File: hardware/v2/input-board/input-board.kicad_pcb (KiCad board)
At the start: 2 copper layers, 110 x 46 mm, 30 parts, among them J27 Screw_Terminal_01x16

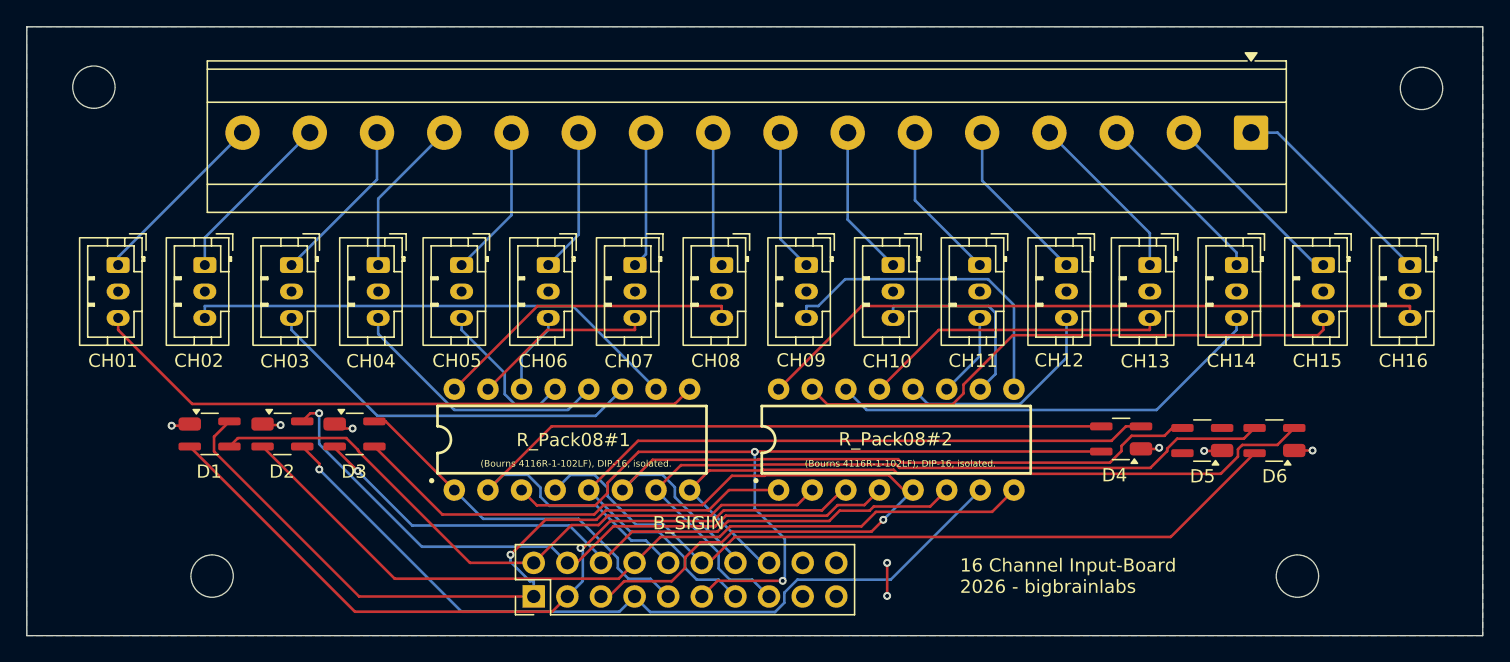
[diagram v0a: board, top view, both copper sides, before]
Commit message: Hardware v2: Input-Board neu generiert (Rev.1/Rev.2)
Gerber neu erzeugt, rev1/rev2-ZIP und Pick-&-Place-CSV ergänzt,
Schaltplan/Layout und Projektdateien aktualisiert.

Co-Authored-By: Claude Opus 4.8 <noreply@anthropic.com>
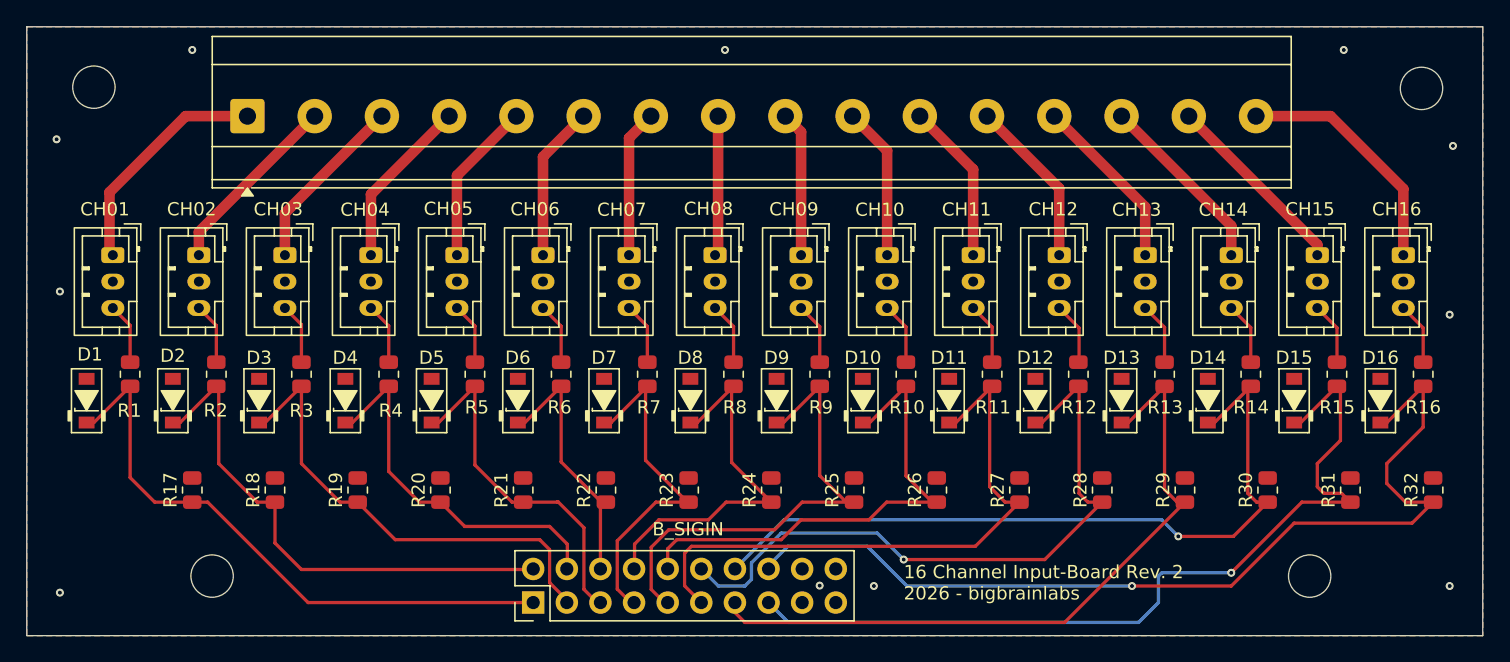
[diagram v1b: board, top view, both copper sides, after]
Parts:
- removed R_Pack08#1, R_Pack08#2: R_Pack08, PCM_SparkFun-Semiconductor-Standard:DIP-16
- added D10: D_Zener, PCM_Diode_SMD_AKL:D_SOD-123_Zener, F.Cu at (166.2, 70.8)
- added D11: D_Zener, PCM_Diode_SMD_AKL:D_SOD-123_Zener, F.Cu at (172.7, 70.8)
- added D12: D_Zener, PCM_Diode_SMD_AKL:D_SOD-123_Zener, F.Cu at (179.2, 70.8)
- added D13: D_Zener, PCM_Diode_SMD_AKL:D_SOD-123_Zener, F.Cu at (185.7, 70.8)
- added D14: D_Zener, PCM_Diode_SMD_AKL:D_SOD-123_Zener, F.Cu at (192.2, 70.8)
- added D15: D_Zener, PCM_Diode_SMD_AKL:D_SOD-123_Zener, F.Cu at (198.8, 70.8)
- added D16: D_Zener, PCM_Diode_SMD_AKL:D_SOD-123_Zener, F.Cu at (205.3, 70.8)
- added D7: D_Zener, PCM_Diode_SMD_AKL:D_SOD-123_Zener, F.Cu at (146.6, 70.8)
- added D8: D_Zener, PCM_Diode_SMD_AKL:D_SOD-123_Zener, F.Cu at (153.1, 70.8)
- added D9: D_Zener, PCM_Diode_SMD_AKL:D_SOD-123_Zener, F.Cu at (159.7, 70.8)
- added R1: 1k, Resistor_SMD:R_0805_2012Metric, F.Cu at (110.8, 68.8)
- added R10: 1k, Resistor_SMD:R_0805_2012Metric, F.Cu at (169.4, 68.8)
- added R11: 1k, Resistor_SMD:R_0805_2012Metric, F.Cu at (175.9, 68.8)
- added R12: 1k, Resistor_SMD:R_0805_2012Metric, F.Cu at (182.4, 68.8)
- added R13: 1k, Resistor_SMD:R_0805_2012Metric, F.Cu at (189.0, 68.8)
- added R14: 1k, Resistor_SMD:R_0805_2012Metric, F.Cu at (195.5, 68.8)
- added R15: 1k, Resistor_SMD:R_0805_2012Metric, F.Cu at (202.0, 68.8)
- added R16: 1k, Resistor_SMD:R_0805_2012Metric, F.Cu at (208.5, 68.8)
- added R17: 1M, Resistor_SMD:R_0805_2012Metric, F.Cu at (115.5, 77.5)
- added R18: 1M, Resistor_SMD:R_0805_2012Metric, F.Cu at (121.8, 77.5)
- added R19: 1M, Resistor_SMD:R_0805_2012Metric, F.Cu at (128.0, 77.5)
- added R2: 1k, Resistor_SMD:R_0805_2012Metric, F.Cu at (117.3, 68.8)
- added R20: 1M, Resistor_SMD:R_0805_2012Metric, F.Cu at (134.2, 77.5)
- added R21: 1M, Resistor_SMD:R_0805_2012Metric, F.Cu at (140.5, 77.5)
- added R22: 1M, Resistor_SMD:R_0805_2012Metric, F.Cu at (146.8, 77.5)
- added R23: 1M, Resistor_SMD:R_0805_2012Metric, F.Cu at (153.0, 77.5)
- added R24: 1M, Resistor_SMD:R_0805_2012Metric, F.Cu at (159.2, 77.5)
- added R25: 1M, Resistor_SMD:R_0805_2012Metric, F.Cu at (165.5, 77.5)
- added R26: 1M, Resistor_SMD:R_0805_2012Metric, F.Cu at (171.8, 77.5)
- added R27: 1M, Resistor_SMD:R_0805_2012Metric, F.Cu at (178.0, 77.5)
- added R28: 1M, Resistor_SMD:R_0805_2012Metric, F.Cu at (184.2, 77.5)
- added R29: 1M, Resistor_SMD:R_0805_2012Metric, F.Cu at (190.5, 77.5)
- added R3: 1k, Resistor_SMD:R_0805_2012Metric, F.Cu at (123.8, 68.8)
- added R30: 1M, Resistor_SMD:R_0805_2012Metric, F.Cu at (196.8, 77.5)
- added R31: 1M, Resistor_SMD:R_0805_2012Metric, F.Cu at (203.0, 77.5)
- added R32: 1M, Resistor_SMD:R_0805_2012Metric, F.Cu at (209.2, 77.5)
- added R4: 1k, Resistor_SMD:R_0805_2012Metric, F.Cu at (130.3, 68.8)
- added R5: 1k, Resistor_SMD:R_0805_2012Metric, F.Cu at (136.9, 68.8)
- added R6: 1k, Resistor_SMD:R_0805_2012Metric, F.Cu at (143.4, 68.8)
- added R7: 1k, Resistor_SMD:R_0805_2012Metric, F.Cu at (149.9, 68.8)
- added R8: 1k, Resistor_SMD:R_0805_2012Metric, F.Cu at (156.4, 68.8)
- added R9: 1k, Resistor_SMD:R_0805_2012Metric, F.Cu at (162.9, 68.8)
- D1, D2, D3, D4, D5, D6: value SP0503BAHTG -> D_Zener; footprint Package_TO_SOT_SMD:SOT-143_Handsoldering -> PCM_Diode_SMD_AKL:D_SOD-123_Zener
- moved CH01 98.0 mm to (109.5, 59.8)
- moved CH16 97.1 mm to (207.0, 59.8)
- moved CH02 85.0 mm to (116.0, 59.8)
- moved CH15 84.1 mm to (200.5, 59.8)
- moved J27 75.8 mm to (119.7, 49.2), turned to 0 degrees
- moved CH03 71.9 mm to (122.5, 59.8)
- moved CH14 71.0 mm to (194.0, 59.8)
- moved CH04 58.9 mm to (129.0, 59.8)
- moved D4 58.7 mm to (127.1, 70.8), turned to 90 degrees
- moved D5 58.3 mm to (133.6, 70.8), turned to 90 degrees
- moved CH13 58.0 mm to (187.5, 59.8)
- moved D6 57.2 mm to (140.1, 70.8), turned to 90 degrees
- moved CH05 46.1 mm to (135.5, 59.8)
- moved CH12 45.2 mm to (181.0, 59.8)
- moved CH06 33.0 mm to (142.0, 59.8)
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- renumbered CH16 to CH01, CH15 to CH02, CH14 to CH03, CH13 to CH04, CH12 to CH05, CH11 to CH06, CH10 to CH07, CH09 to CH08, CH08 to CH09, CH07 to CH10, CH06 to CH11, CH05 to CH12, CH04 to CH13, CH03 to CH14, CH02 to CH15, CH01 to CH16
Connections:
- B_SIGIN pad 1: Net-(J29-Pin_1) -> Net-(D1-K)
- B_SIGIN pad 10: Net-(J29-Pin_10) -> Net-(D10-K)
- B_SIGIN pad 11: Net-(J29-Pin_11) -> Net-(D11-K)
- B_SIGIN pad 12: Net-(J29-Pin_12) -> Net-(D12-K)
- B_SIGIN pad 13: Net-(J29-Pin_13) -> Net-(D13-K)
- B_SIGIN pad 14: Net-(J29-Pin_14) -> Net-(D14-K)
- B_SIGIN pad 15: Net-(J29-Pin_15) -> Net-(D15-K)
- B_SIGIN pad 16: Net-(J29-Pin_16) -> Net-(D16-K)
- B_SIGIN pad 2: Net-(J29-Pin_2) -> Net-(D2-K)
- B_SIGIN pad 3: Net-(J29-Pin_3) -> Net-(D3-K)
- B_SIGIN pad 4: Net-(J29-Pin_4) -> Net-(D4-K)
- B_SIGIN pad 5: Net-(J29-Pin_5) -> Net-(D5-K)
- B_SIGIN pad 6: Net-(J29-Pin_6) -> Net-(D6-K)
- B_SIGIN pad 7: Net-(J29-Pin_7) -> Net-(D7-K)
- B_SIGIN pad 8: Net-(J29-Pin_8) -> Net-(D8-K)
- B_SIGIN pad 9: Net-(J29-Pin_9) -> Net-(D9-K)
- D1 pad 1: GND -> Net-(D1-K)
- D1 pad 2: Net-(J29-Pin_3) -> GND
- D2 pad 1: GND -> Net-(D2-K)
- D2 pad 2: Net-(J29-Pin_8) -> GND
- D3 pad 1: GND -> Net-(D3-K)
- D3 pad 2: Net-(J29-Pin_6) -> GND
- D4 pad 1: GND -> Net-(D4-K)
- D4 pad 2: Net-(J29-Pin_13) -> GND
- D5 pad 1: GND -> Net-(D5-K)
- D5 pad 2: unconnected-(D5-Pad2) -> GND
- D6 pad 1: GND -> Net-(D6-K)
- D6 pad 2: Net-(J29-Pin_16) -> GND
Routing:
- net Net-(J29-Pin_5): track 71.9 -> 0.00 mm, vias 1 -> 0
- net Net-(D16-K): track 0.00 -> 71.9 mm, vias 0 -> 1
- net Net-(J29-Pin_10): track 65.6 -> 0.00 mm
- net Net-(D15-K): track 0.00 -> 65.3 mm, vias 0 -> 1
- net Net-(J29-Pin_11): track 63.8 -> 0.00 mm, vias 2 -> 0
- net Net-(J29-Pin_8): track 63.7 -> 0.00 mm
- net Net-(J29-Pin_7): track 61.9 -> 0.00 mm, vias 1 -> 0
- net Net-(J29-Pin_3): track 60.3 -> 0.00 mm, vias 1 -> 0
- net Net-(J29-Pin_15): track 60.1 -> 0.00 mm
- net Net-(J29-Pin_12): track 59.9 -> 0.00 mm
- net Net-(J29-Pin_13): track 58.6 -> 0.00 mm
- net Net-(J29-Pin_1): track 57.8 -> 0.00 mm, vias 1 -> 0
- net Net-(D14-K): track 0.00 -> 57.7 mm, vias 0 -> 1
- net Net-(J29-Pin_14): track 57.1 -> 0.00 mm
- net Net-(J29-Pin_16): track 56.5 -> 0.00 mm
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- added copper zone on F.Cu, net GND
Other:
- board text added: "16 Channel Input-Board Rev. 2 2026 - bigbrainlabs"
- board text removed: "(Bourns 4116R-1-102LF), DIP-16, isolated."
- board text removed: "16 Channel Input-Board 2026 - bigbrainlabs"

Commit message: Hardware: Gerber & KiCad-Projektdateien aktualisiert
MotorCombo_THT und v2/input-board: Gerber, Bohrdateien, ZIP,
Bestueckungs-CSV und KiCad-Projektdateien neu erzeugt.

Co-Authored-By: Claude Opus 4.8 <noreply@anthropic.com>
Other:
- board text added: "sponsored by"
